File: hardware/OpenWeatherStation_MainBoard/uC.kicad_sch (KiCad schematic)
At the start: 1 part, among them U1 STM32F107VCTx

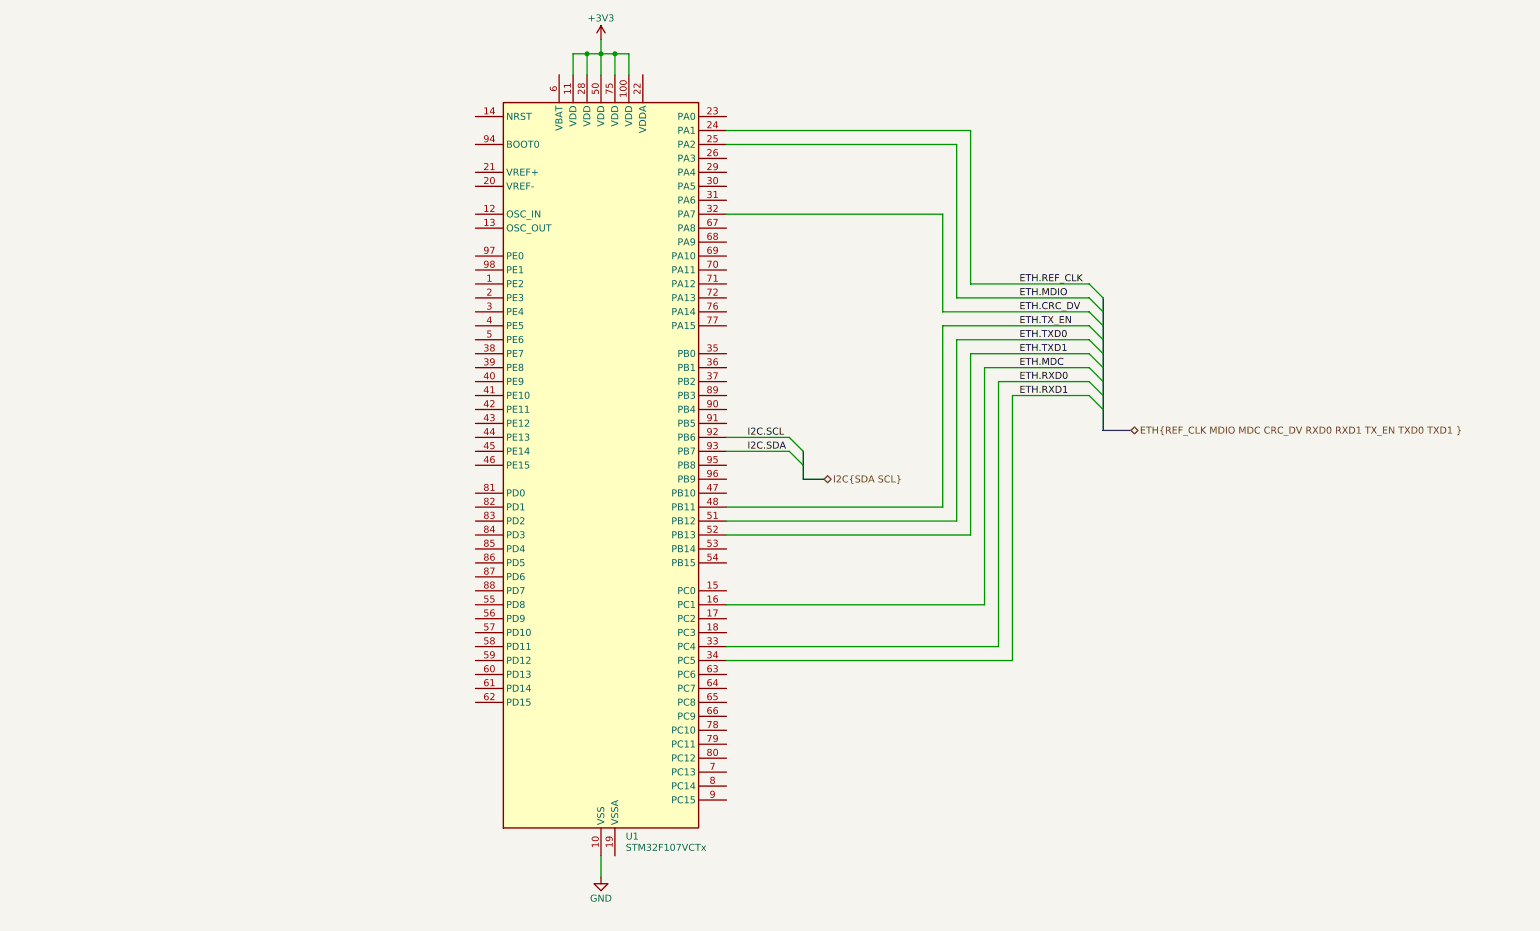
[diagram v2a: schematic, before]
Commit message: update schematic
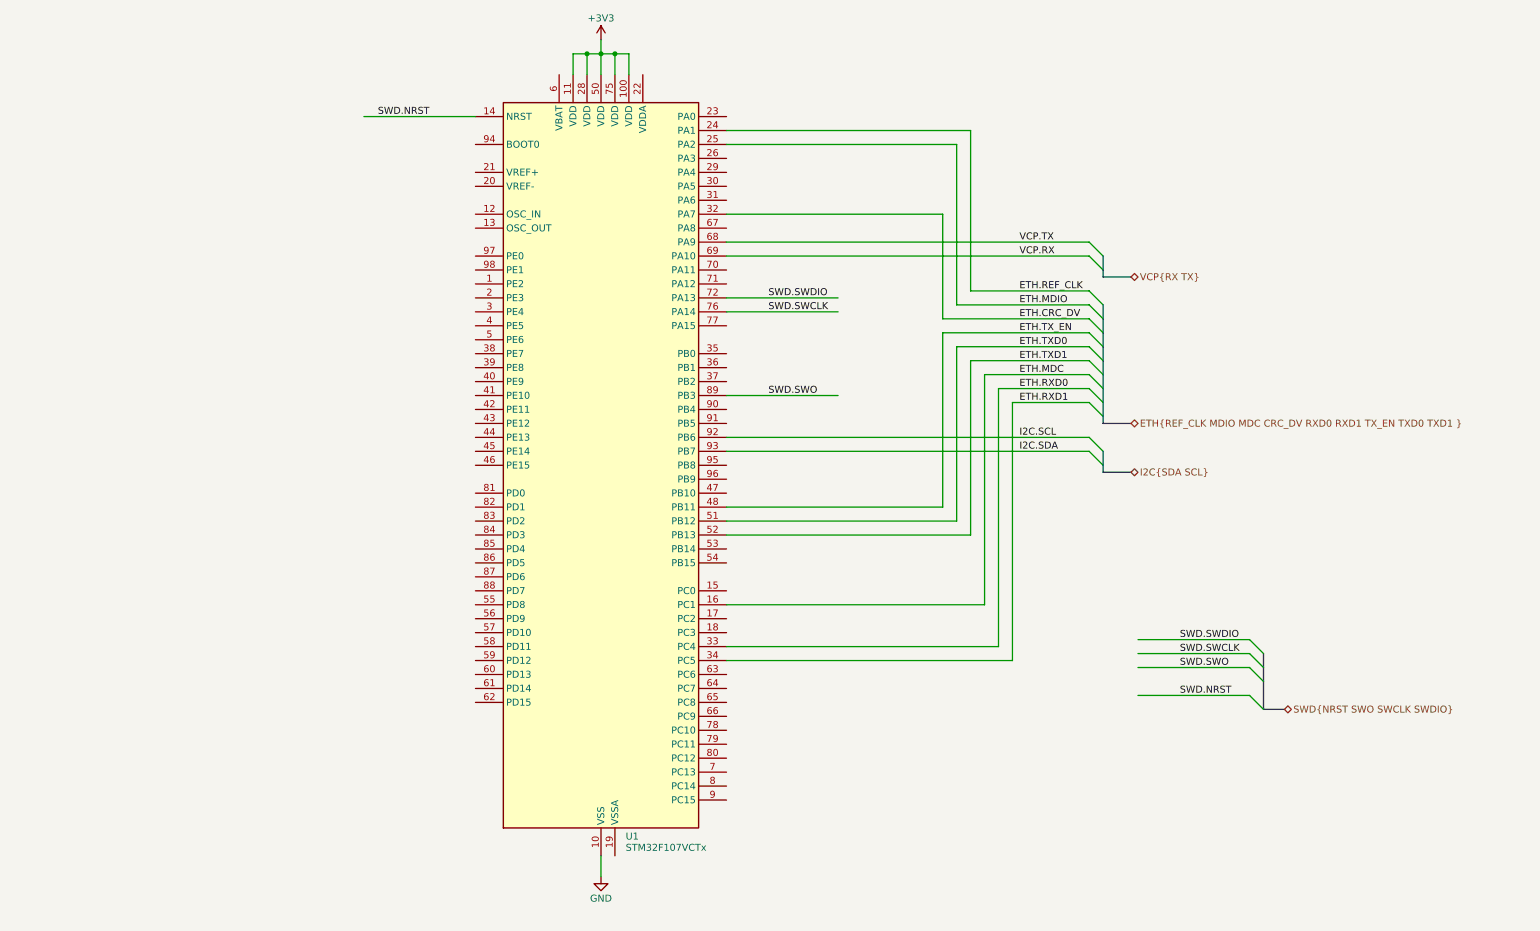
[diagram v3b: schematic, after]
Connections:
- net SWD.NRST: now reaches U1.14 (NRST)
- net VCP.TX: now reaches U1.68 (PA9)
- net VCP.RX: now reaches U1.69 (PA10)
- net SWD.SWDIO: now reaches U1.72 (PA13)
- net SWD.SWCLK: now reaches U1.76 (PA14)
- net SWD.SWO: now reaches U1.89 (PB3)

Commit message: schematic update
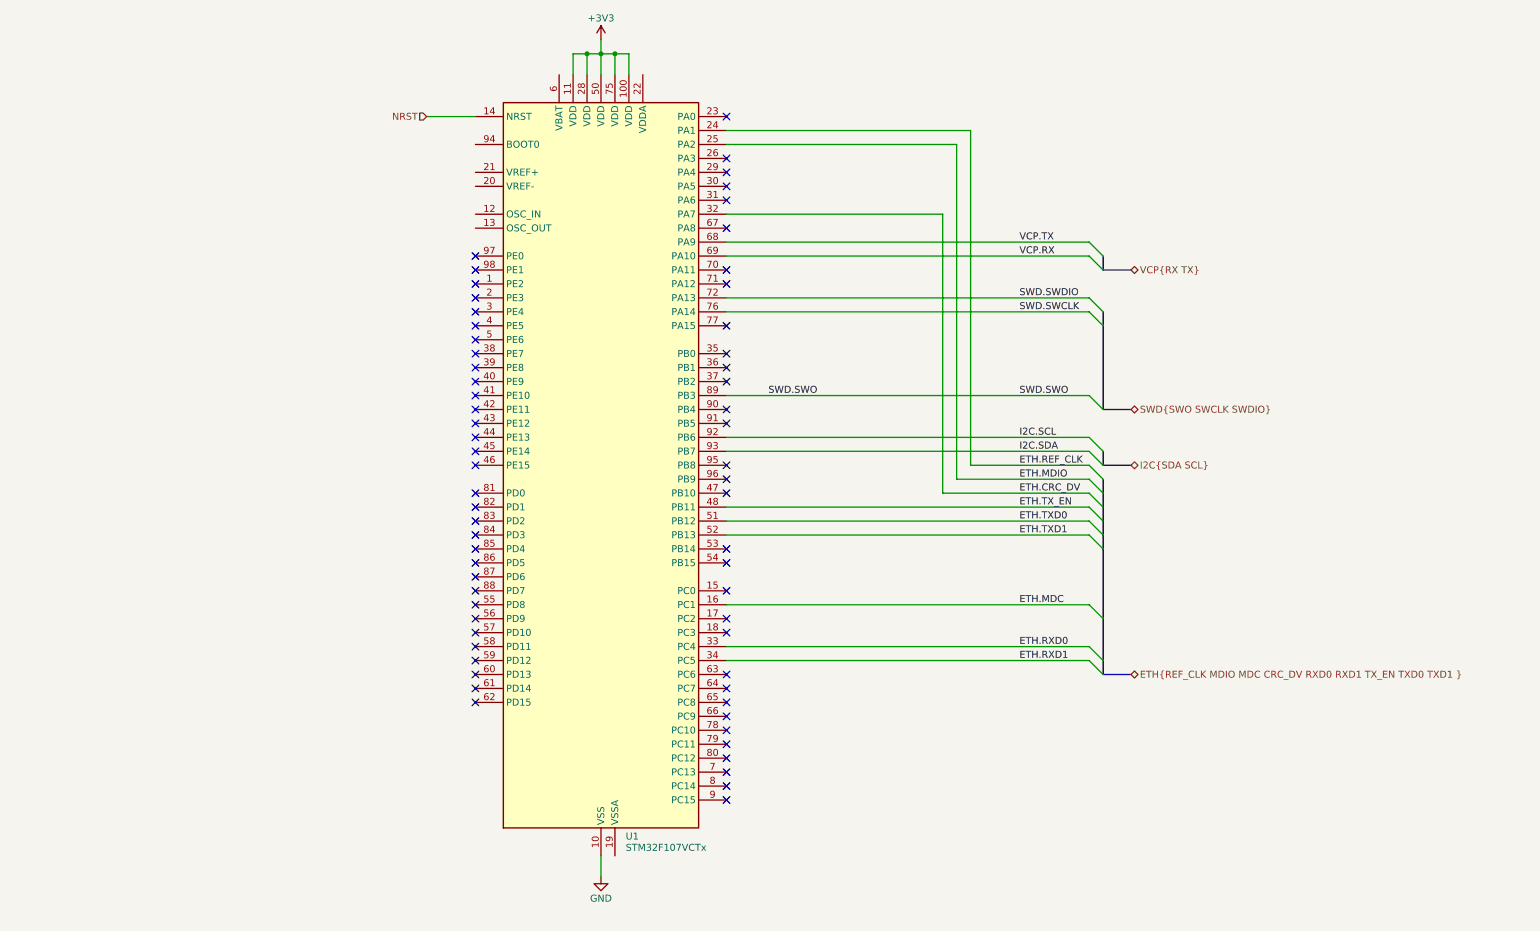
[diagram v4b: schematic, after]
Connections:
- net SWD.NRST renamed NRST
- no-connect marks 0 -> 64

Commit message: electrical design wip
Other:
- company: (none) -> Vital Septfonds
- title: (none) -> Open Wheather Station
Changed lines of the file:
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@@
 (kicad_sch (version 20230121) (generator eeschema)
   (paper "A4")
+  (title_block
+    (title "Open Wheather Station")
+    (date "2024-01-02")
+    (rev "1.0")
+    (company "Vital Septfonds")
+  )
   (junction (at 124.46 24.13) (diameter 0) (color 0 0 0 0)
   )

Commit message: update elec
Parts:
- added FB2: FerriteBead, symbol Device:FerriteBead
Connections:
- net +3V3: now also U1.6 (VBAT), FB2.1
- net GND: now also U1.19 (VSSA)
- net +3.3VA: now reaches U1.21 (VREF+)
- net +3.3VA: now also U1.22 (VDDA), FB2.2
- no-connect marks 64 -> 68
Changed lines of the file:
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@@
   (junction (at 121.92 24.13) (diameter 0) (color 0 0 0 0)
+  )
+  (junction (at 116.84 24.13) (diameter 0) (color 0 0 0 0)
+  )
+  (junction (at 129.54 25.4) (diameter 0) (color 0 0 0 0)
+  )
+  (junction (at 121.92 171.45) (diameter 0) (color 0 0 0 0)
   )
   (junction (at 119.38 24.13) (diameter 0) (color 0 0 0 0)
@@
   (no_connect (at 99.06 104.14))
   (no_connect (at 144.78 104.14))
+  (no_connect (at 99.06 53.34))
   (no_connect (at 99.06 137.16))
+  (no_connect (at 99.06 40.64))
   (no_connect (at 144.78 99.06))
   (no_connect (at 99.06 86.36))
@@
   (no_connect (at 144.78 35.56))
   (no_connect (at 99.06 93.98))
+  (no_connect (at 99.06 48.26))
   (no_connect (at 99.06 76.2))
   (no_connect (at 99.06 68.58))
@@
   (no_connect (at 99.06 60.96))
   (no_connect (at 99.06 121.92))
+  (no_connect (at 99.06 55.88))
   (no_connect (at 144.78 101.6))
   (bus_entry (at 210.82 132.08) (size 2.54 2.54)
@@
     (stroke (width 0) (type default))
   )
+  (wire (pts (xy 199.39 27.94) (xy 191.77 27.94))
+    (stroke (width 0) (type default))
+  )
   (wire (pts (xy 144.78 60.96) (xy 210.82 60.96))
     (stroke (width 0) (type default))
   )
+  (wire (pts (xy 124.46 171.45) (xy 121.92 171.45))
+    (stroke (width 0) (type default))
+  )
+  (wire (pts (xy 114.3 24.13) (xy 114.3 27.94))
+    (stroke (width 0) (type default))
+  )
   (bus (pts (xy 213.36 88.9) (xy 218.44 88.9))
     (stroke (width 0) (type default))
@@
     (stroke (width 0) (type default))
   )
+  (wire (pts (xy 129.54 25.4) (xy 129.54 22.86))
+    (stroke (width 0) (type default))
+  )
   (bus (pts (xy 213.36 114.3) (xy 213.36 111.76))
     (stroke (width 0) (type default))
   )
-  (wire (pts (xy 121.92 170.18) (xy 121.92 173.99))
+  (wire (pts (xy 121.92 170.18) (xy 121.92 171.45))
     (stroke (width 0) (type default))
   )
@@
     (stroke (width 0) (type default))
   )
+  (wire (pts (xy 90.17 45.72) (xy 99.06 45.72))
+    (stroke (width 0) (type default))
+  )
   (wire (pts (xy 186.69 101.6) (xy 186.69 40.64))
     (stroke (width 0) (type default))
@@
     (stroke (width 0) (type default))
   )
+  (wire (pts (xy 215.9 25.4) (xy 215.9 27.94))
+    (stroke (width 0) (type default))
+  )
   (wire (pts (xy 127 27.94) (xy 127 24.13))
     (stroke (width 0) (type default))
@@
     (stroke (width 0) (type default))
   )
+  (wire (pts (xy 121.92 171.45) (xy 121.92 173.99))
+    (stroke (width 0) (type default))
+  )
   (wire (pts (xy 144.78 106.68) (xy 210.82 106.68))
     (stroke (width 0) (type default))
@@
     (stroke (width 0) (type default))
   )
+  (wire (pts (xy 116.84 24.13) (xy 114.3 24.13))
+    (stroke (width 0) (type default))
+  )
+  (wire (pts (xy 207.01 27.94) (xy 215.9 27.94))
+    (stroke (width 0) (type default))
+  )
   (bus (pts (xy 213.36 99.06) (xy 218.44 99.06))
     (stroke (width 0) (type default))
@@
     (stroke (width 0) (type default))
   )
+  (wire (pts (xy 124.46 170.18) (xy 124.46 171.45))
+    (stroke (width 0) (type default))
+  )
   (wire (pts (xy 124.46 24.13) (xy 124.46 27.94))
     (stroke (width 0) (type default))
   )
+  (wire (pts (xy 191.77 27.94) (xy 191.77 25.4))
+    (stroke (width 0) (type default))
+  )
   (bus (pts (xy 213.36 96.52) (xy 213.36 99.06))
+    (stroke (width 0) (type default))
+  )
+  (wire (pts (xy 129.54 27.94) (xy 129.54 25.4))
     (stroke (width 0) (type default))
   )
@@
     (effects (font (size 1.27 1.27)) (justify left))
   )
+  (symbol (lib_id "power:+3.3VA") (at 215.9 25.4 0) (unit 1)
+    (in_bom yes) (on_board yes) (dnp no) (fields_autoplaced)
+    (property "Reference" "#PWR025" (at 215.9 29.21 0)
+      (effects (font (size 1.27 1.27)) hide)
+    )
+    (property "Value" "+3.3VA" (at 215.9 20.32 0)
+      (effects (font (size 1.27 1.27)))
+    )
+    (property "Footprint" "" (at 215.9 25.4 0)
+      (effects (font (size 1.27 1.27)) hide)
+    )
+    (property "Datasheet" "" (at 215.9 25.4 0)
+      (effects (font (size 1.27 1.27)) hide)
+    )
+    (pin "1")
+    (instances
+      (project "OpenWeatherStation_MainBoard"
+        (path "/698c4dde-56a2-4dd1-89d2-180a09a5dfe9/ecef3463-8a76-4601-aba2-c0b4af8f7f37"
+          (reference "#PWR025") (unit 1)
+        )
+      )
+    )
+  )
+  (symbol (lib_id "power:+3V3") (at 191.77 25.4 0) (unit 1)
+    (in_bom yes) (on_board yes) (dnp no) (fields_autoplaced)
+    (property "Reference" "#PWR09" (at 191.77 29.21 0)
+      (effects (font (size 1.27 1.27)) hide)
+    )
+    (property "Value" "+3V3" (at 191.77 21.455 0)
+      (effects (font (size 1.27 1.27)))
+    )
+    (property "Footprint" "" (at 191.77 25.4 0)
+      (effects (font (size 1.27 1.27)) hide)
+    )
+    (property "Datasheet" "" (at 191.77 25.4 0)
+      (effects (font (size 1.27 1.27)) hide)
+    )
+    (pin "1")
+    (instances
+      (project "OpenWeatherStation_MainBoard"
+        (path "/698c4dde-56a2-4dd1-89d2-180a09a5dfe9/ecef3463-8a76-4601-aba2-c0b4af8f7f37"
+          (reference "#PWR09") (unit 1)
+        )
+      )
+    )
+  )
   (symbol (lib_id "power:GND") (at 121.92 173.99 0) (unit 1)
     (in_bom yes) (on_board yes) (dnp no) (fields_autoplaced)
@@
         (path "/698c4dde-56a2-4dd1-89d2-180a09a5dfe9/ecef3463-8a76-4601-aba2-c0b4af8f7f37"
           (reference "#PWR08") (unit 1)
+        )
+      )
+    )
+  )
+  (symbol (lib_id "power:PWR_FLAG") (at 129.54 25.4 270) (unit 1)
+    (in_bom yes) (on_board yes) (dnp no) (fields_autoplaced)
+    (property "Reference" "#FLG08" (at 131.445 25.4 0)
+      (effects (font (size 1.27 1.27)) hide)
+    )
+    (property "Value" "PWR_FLAG" (at 133.35 25.4 90)
+      (effects (font (size 1.27 1.27)) (justify left))
+    )
+    (property "Footprint" "" (at 129.54 25.4 0)
+      (effects (font (size 1.27 1.27)) hide)
+    )
+    (property "Datasheet" "~" (at 129.54 25.4 0)
+      (effects (font (size 1.27 1.27)) hide)
+    )
+    (pin "1")
+    (instances
+      (project "OpenWeatherStation_MainBoard"
+        (path "/698c4dde-56a2-4dd1-89d2-180a09a5dfe9/ecef3463-8a76-4601-aba2-c0b4af8f7f37"
+          (reference "#FLG08") (unit 1)
         )
       )
@@
         )
       )
+    )
+  )
+  (symbol (lib_id "power:+3.3VA") (at 90.17 45.72 0) (unit 1)
+    (in_bom yes) (on_board yes) (dnp no) (fields_autoplaced)
+    (property "Reference" "#PWR038" (at 90.17 49.53 0)
+      (effects (font (size 1.27 1.27)) hide)
+    )
+    (property "Value" "+3.3VA" (at 90.17 40.64 0)
+      (effects (font (size 1.27 1.27)))
+    )
+    (property "Footprint" "" (at 90.17 45.72 0)
+      (effects (font (size 1.27 1.27)) hide)
+    )
+    (property "Datasheet" "" (at 90.17 45.72 0)
+      (effects (font (size 1.27 1.27)) hide)
+    )
+    (pin "1")
+    (instances
+      (project "OpenWeatherStation_MainBoard"
+        (path "/698c4dde-56a2-4dd1-89d2-180a09a5dfe9/ecef3463-8a76-4601-aba2-c0b4af8f7f37"
+          (reference "#PWR038") (unit 1)
+        )
+      )
+    )
+  )
+  (symbol (lib_id "Device:FerriteBead") (at 203.2 27.94 90) (unit 1)
+    (in_bom yes) (on_board yes) (dnp no) (fields_autoplaced)
+    (property "Reference" "FB2" (at 203.1492 20.32 90)
+      (effects (font (size 1.27 1.27)))
+    )
+    (property "Value" "FerriteBead" (at 203.1492 22.86 90)
+      (effects (font (size 1.27 1.27)))
+    )
+    (property "Footprint" "" (at 203.2 29.718 90)
+      (effects (font (size 1.27 1.27)) hide)
+    )
+    (property "Datasheet" "~" (at 203.2 27.94 0)
+      (effects (font (size 1.27 1.27)) hide)
+    )
+    (pin "1")
+    (pin "2")
+    (instances
+      (project "OpenWeatherStation_MainBoard"
+        (path "/698c4dde-56a2-4dd1-89d2-180a09a5dfe9/ecef3463-8a76-4601-aba2-c0b4af8f7f37"
+          (reference "FB2") (unit 1)
+        )
+      )
+    )
+  )
+  (symbol (lib_id "power:+3.3VA") (at 129.54 22.86 0) (unit 1)
+    (in_bom yes) (on_board yes) (dnp no) (fields_autoplaced)
+    (property "Reference" "#PWR010" (at 129.54 26.67 0)
+      (effects (font (size 1.27 1.27)) hide)
+    )
+    (property "Value" "+3.3VA" (at 129.54 17.78 0)
+      (effects (font (size 1.27 1.27)))
+    )
+    (property "Footprint" "" (at 129.54 22.86 0)
+      (effects (font (size 1.27 1.27)) hide)
+    )
+    (property "Datasheet" "" (at 129.54 22.86 0)
+      (effects (font (size 1.27 1.27)) hide)
+    )
+    (pin "1")
+    (instances
+      (project "OpenWeatherStation_MainBoard"
+        (path "/698c4dde-56a2-4dd1-89d2-180a09a5dfe9/ecef3463-8a76-4601-aba2-c0b4af8f7f37"
+          (reference "#PWR010") (unit 1)
+        )
+      )

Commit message: udpate pcb design
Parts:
- added C1, C2, C3, C4, C5, C9: 100nF, Capacitor_SMD:C_0603_1608Metric, symbol Device:C
- FB2: footprint (none) -> Capacitor_SMD:C_0603_1608Metric
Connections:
- net +3V3: now also C1.1, C2.1, C3.1, C4.1, C5.1, C9.1
- net GND: now also C1.2, C2.2, C3.2, C4.2, C5.2, C9.2
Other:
- moved on the sheet: FB2, U1
